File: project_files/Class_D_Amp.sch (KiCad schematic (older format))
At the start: 81 parts, among them P1 ROUT, P2 LOUT, P3 CONN_01X04, P4 2x12V, Q1 BC847, Q2 BC857, Q3 IPD180N10, Q4 IPD180N10, Q5 IPD180N10, Q6 IPD180N10, U1 LM360, U2 UCC27201, U3 LM833, U4 IES101-4, U5 LM360, U6 UCC27201

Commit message: Updated schematic and netlist
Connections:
- net VSS: now also C33.2; no longer C33.1
- net VSS+12V: now also C33.1; no longer C33.2
- net at L1.1, Q3.3 (S), Q4.2 (D)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: now also C7.1, C7.2, U2.2 (HB), U2.4 (HS)
- net at L2.1, Q5.3 (S), Q6.2 (D)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: now also C19.1, C19.2, U6.2 (HB), U6.4 (HS)

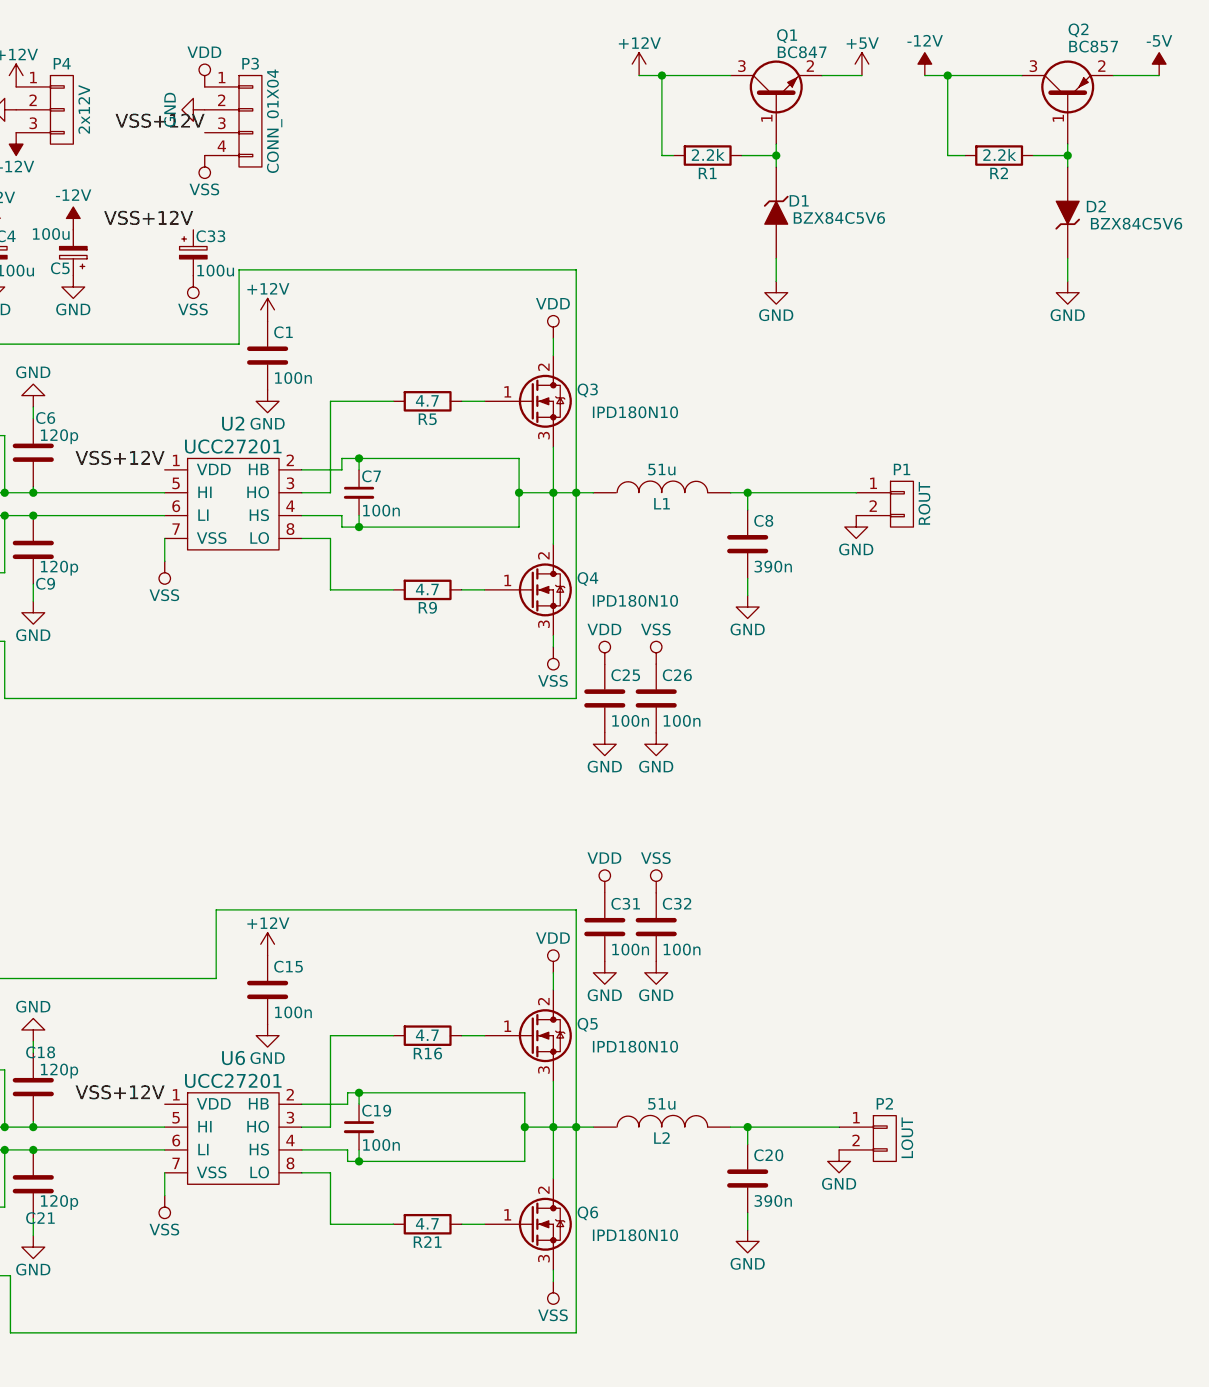
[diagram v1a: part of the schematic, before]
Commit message: Clustered modules together
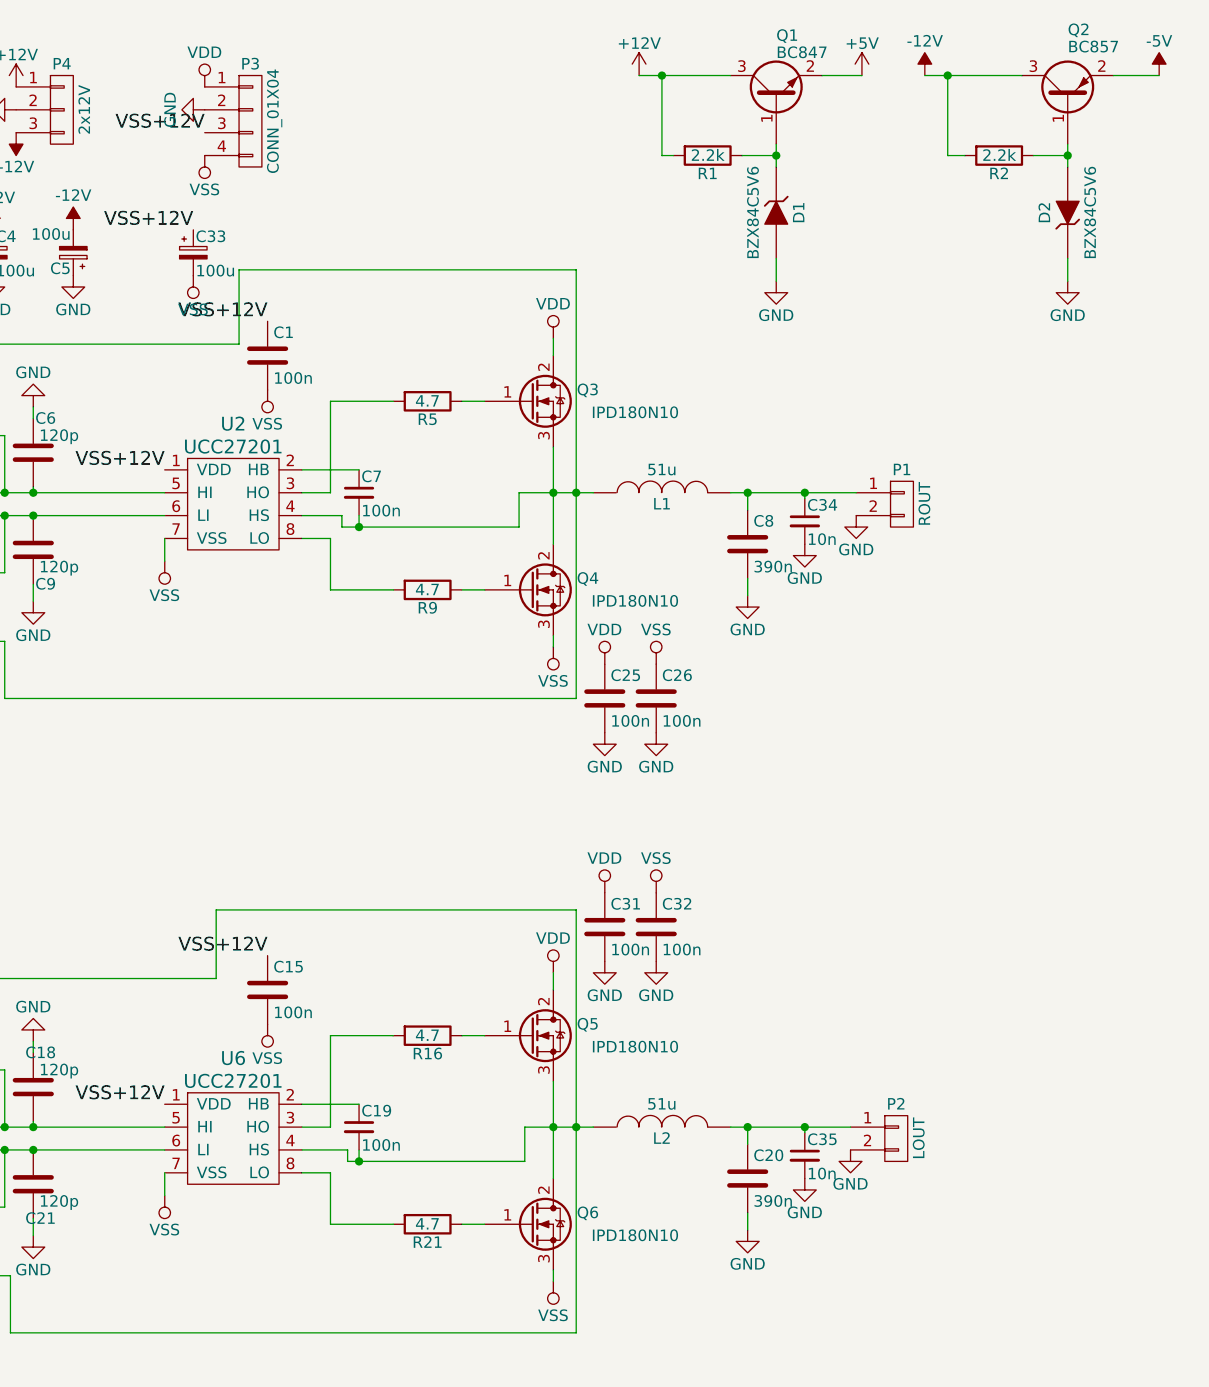
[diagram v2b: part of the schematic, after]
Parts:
- removed D1, D2: BZX84C5V6, TO_SOT_Packages_SMD:SOT-23, symbol ZENER
- added C34, C35: 10n, Capacitors_SMD:C_0805, symbol C_Small
- added D1, D2: BZX84C5V6, TO_SOT_Packages_SMD:SOT-23, symbol BZX84C5V6
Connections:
- net +12V: no longer C1.1, C15.1
- net GND: now also C34.2, C35.2, D1.1 (A), D2.3 (K); no longer C1.2, C15.2
- net VSS: now also C1.2, C15.2
- net VSS+12V: now also C1.1, C15.1
- net at C7.2, L1.1, Q3.3 (S)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: no longer C7.1, U2.2 (HB)
- net at C8.1, L1.2, P1.1 (P1): now also C34.1
- net at Q1.1 (B), R1.1: now also D1.3 (K)
- net at Q2.1 (B), R2.1: now also D2.1 (A)
- net at C19.2, L2.1, Q5.3 (S)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: no longer C19.1, U6.2 (HB)
- net at C20.1, L2.2, P2.1 (P1): now also C35.1
- new net: C7.1, U2.2 (HB)
- new net: C19.1, U6.2 (HB)
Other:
- moved on the sheet: P2

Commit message: Updated PCB design
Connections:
- net RNODE: now reaches C7.2, L1.1, Q3.3 (S), Q4.2 (D), R10.1, R4.1, U2.4 (HS)
- net ROUT: now reaches C34.1, C8.1, L1.2, P1.1 (P1)
- net LNODE: now reaches C19.2, L2.1, Q5.3 (S), Q6.2 (D), R15.1, R22.1, U6.4 (HS)
- net LOUT: now reaches C20.1, C35.1, L2.2, P2.1 (P1)
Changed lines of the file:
@@
 	9550 5400 9550 5425
 Connection ~ 9550 5400
+Text Label 9425 2625 0    60   ~ 0
+ROUT
+Text Label 9425 5400 0    60   ~ 0
+LOUT
+Text Label 8500 5400 0    60   ~ 0
+LNODE
+Text Label 8500 2625 0    60   ~ 0
+RNODE
 $EndSCHEMATC

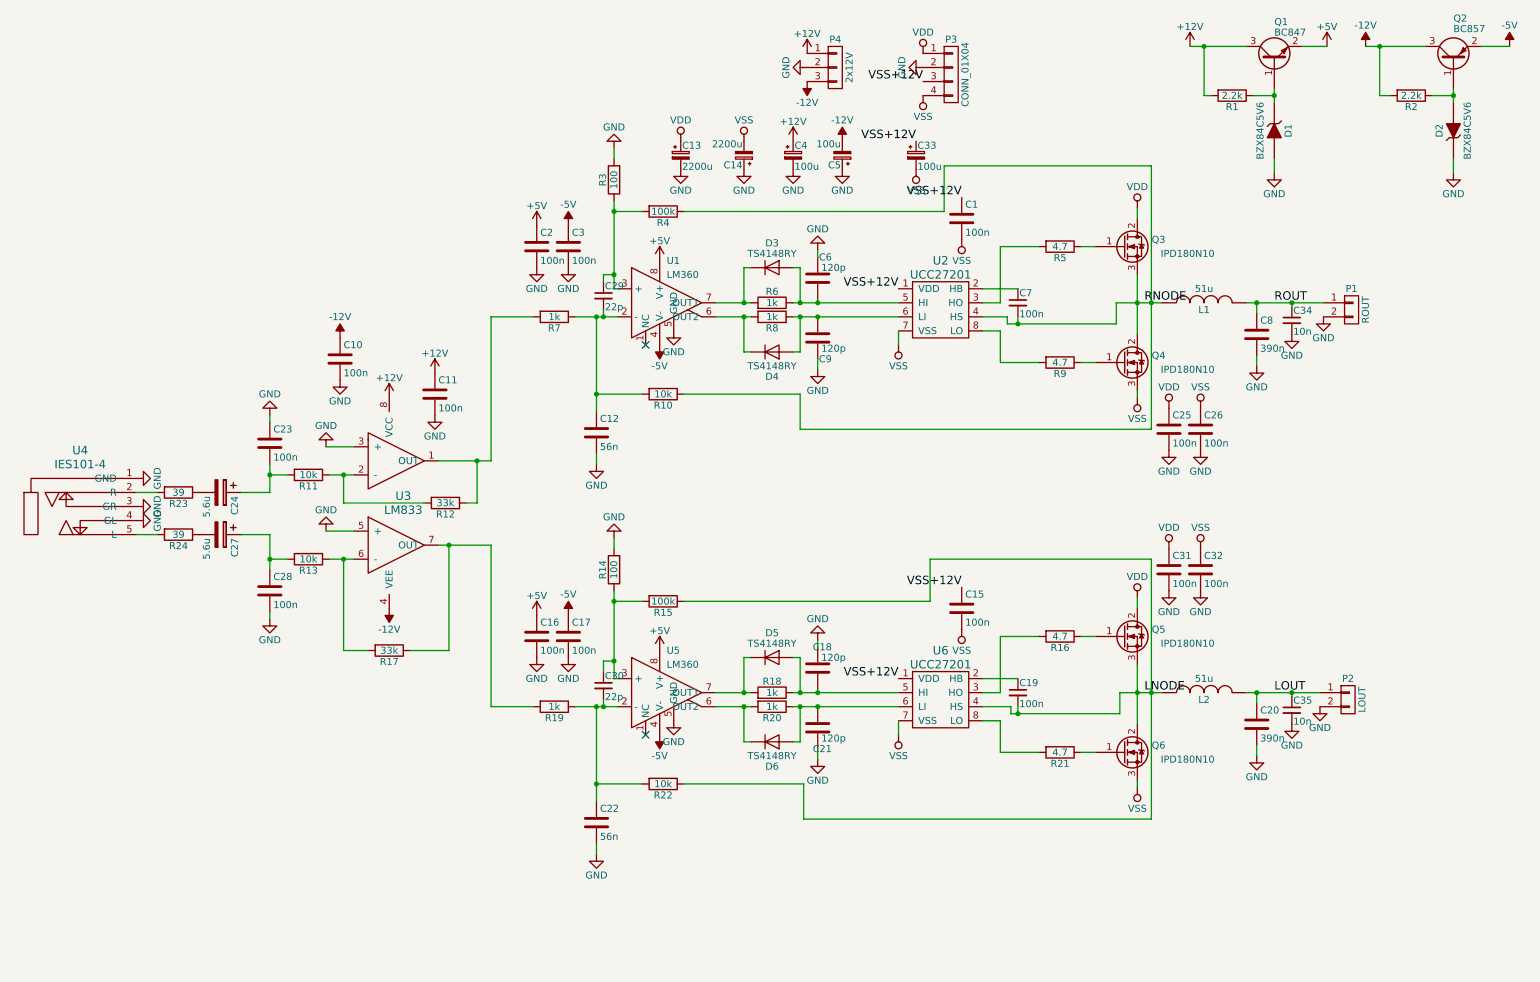
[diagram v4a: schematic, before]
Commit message: Added the Level Shifters to Schematic
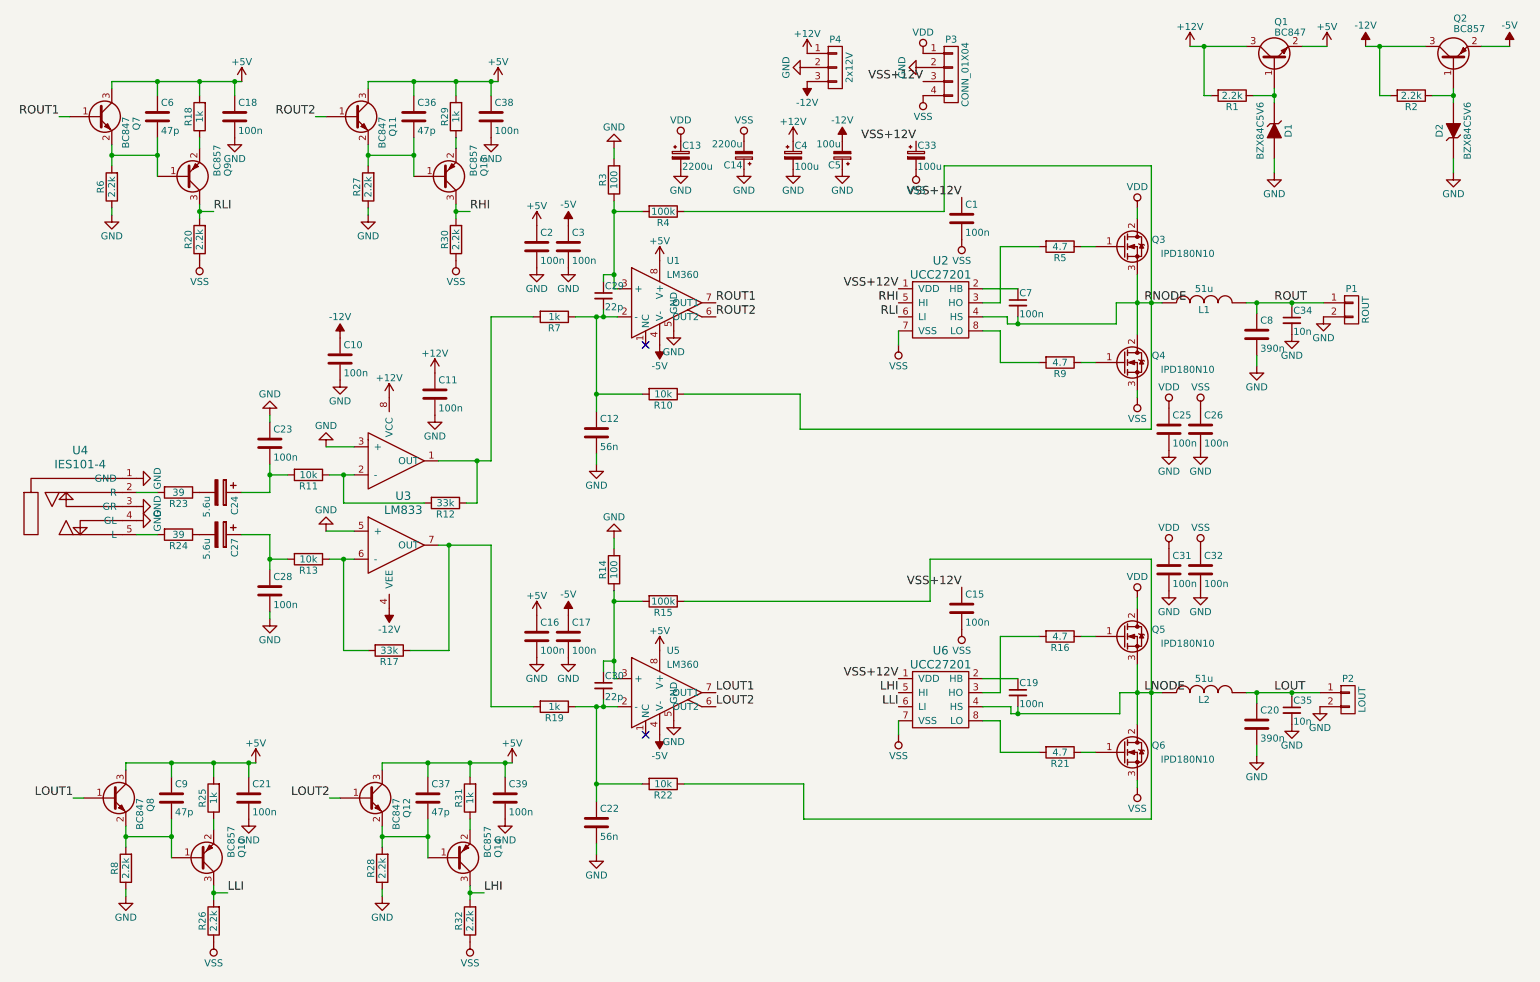
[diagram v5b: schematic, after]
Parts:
- removed D3, D4, D5, D6: TS4148RY, Diodes_SMD:D_0805, symbol D
- added C36, C37: 47p, Capacitors_SMD:C_0805, symbol C
- added C38, C39: 100n, Capacitors_SMD:C_0805, symbol C
- added Q10, Q13, Q14, Q9: BC857, TO_SOT_Packages_SMD:SOT-23, symbol Q_PNP_BEC
- added Q11, Q12, Q7, Q8: BC847, TO_SOT_Packages_SMD:SOT-23, symbol Q_NPN_BEC
- added R25, R29, R31: 1k, Resistors_SMD:R_0805, symbol R
- added R26, R27, R28, R30, R32: 2.2k, Resistors_SMD:R_0805, symbol R
- C18, C21: value 120p -> 100n
- C6, C9: value 120p -> 47p
- R20, R6, R8: value 1k -> 2.2k
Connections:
- net +5V: now also C18.1, C21.1, C6.1, C9.1, R18.2, C36.1, C37.1, C38.1, C39.1, Q11.3 (C), Q12.3 (C), Q7.3 (C), Q8.3 (C), R25.2, R29.2, R31.2
- net GND: now also R6.1, R8.1, C38.2, C39.2, R27.1, R28.1; no longer C6.2, C9.2
- net VSS: now also R20.1, R26.1, R30.1, R32.1
- net at R8.2: now also C9.2, Q10.1 (B), Q8.2 (E); no longer U1.6 (OUT2)
- net at R6.2: now also C6.2, Q7.2 (E), Q9.1 (B); no longer U1.7 (OUT1)
- net LOUT2: now reaches U5.6 (OUT2)
- net LOUT2: now also Q12.1 (B); no longer R20.2
- net LOUT1: now reaches U5.7 (OUT1)
- net LOUT1: now also Q8.1 (B); no longer R18.2
- new net: Q10.2 (E), R25.1
- new net: C37.2, Q12.2 (E), Q14.1 (B), R28.2
- new net: Q14.2 (E), R31.1
- new net: Q9.2 (E), R18.1
- new net: C36.2, Q11.2 (E), Q13.1 (B), R27.2
- new net: Q13.2 (E), R29.1
- new net LHI: Q14.3 (C), R32.2, U6.5 (HI)
- new net LLI: Q10.3 (C), R26.2, U6.6 (LI)
- new net RHI: Q13.3 (C), R30.2, U2.5 (HI)
- new net RLI: Q9.3 (C), R20.2, U2.6 (LI)
- new net ROUT1: Q7.1 (B), U1.7 (OUT1)
- new net ROUT2: Q11.1 (B), U1.6 (OUT2)
